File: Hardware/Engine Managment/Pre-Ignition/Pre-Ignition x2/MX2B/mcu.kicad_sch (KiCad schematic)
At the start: 2 parts

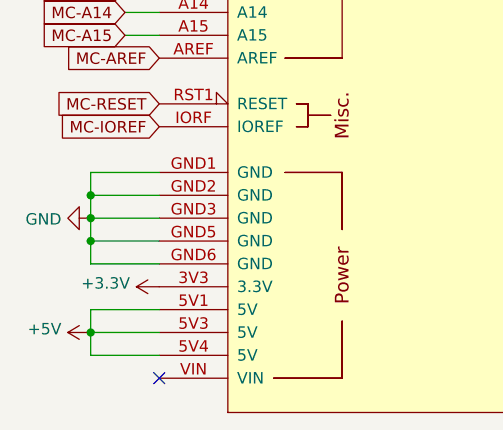
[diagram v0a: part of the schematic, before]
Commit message: schematic exports
kicad version updates, schematic exports
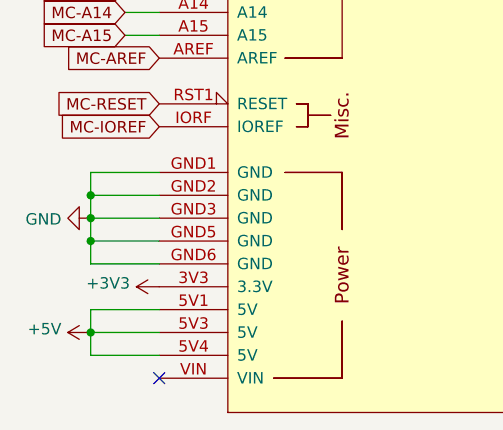
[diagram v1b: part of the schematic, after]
